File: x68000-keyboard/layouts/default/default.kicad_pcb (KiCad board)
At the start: 2 copper layers, 29.6 x 12.2 mm, 19 parts

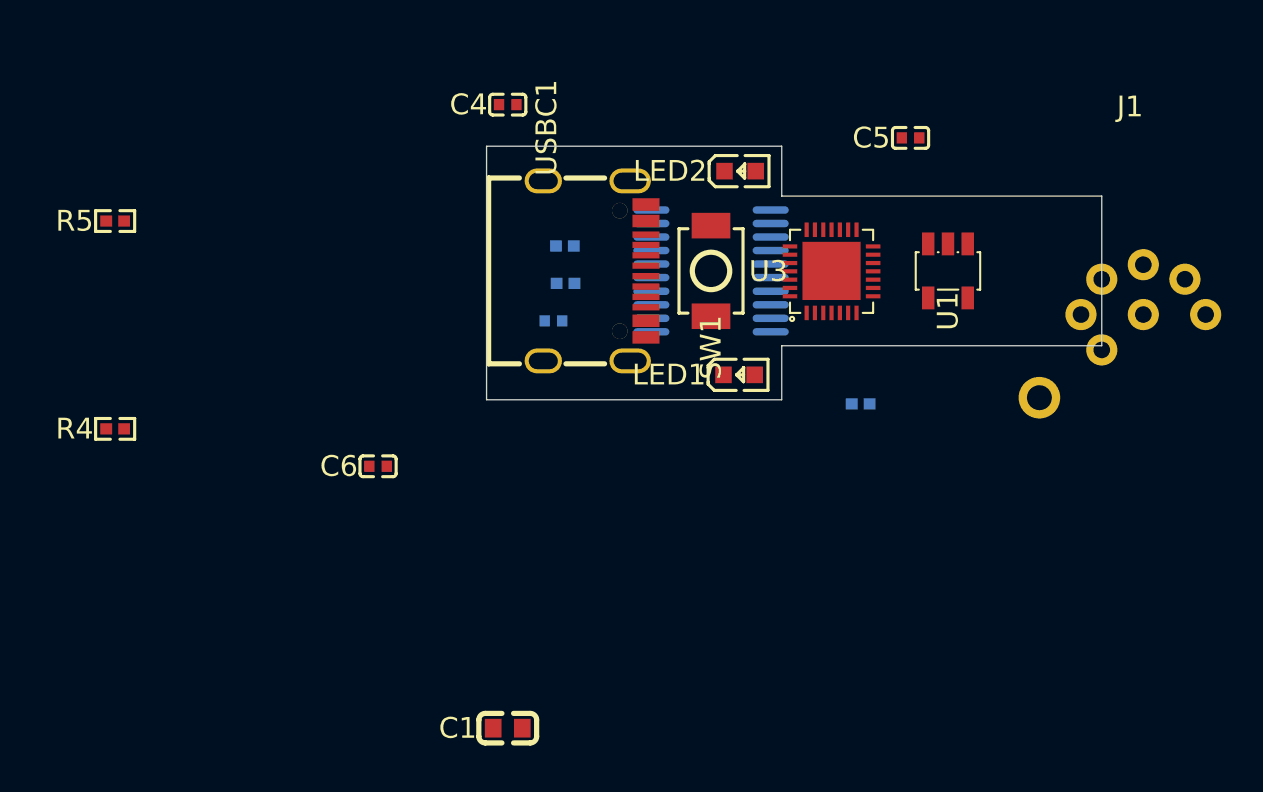
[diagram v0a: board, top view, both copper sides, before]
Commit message: x68000-keyboard: デバッグ LED 削除と Mini-DIN 7pin 自作部品化
- 基板を小型化するためデバッグ LED 2 個と直列抵抗 2 個を削除
  (PB3 / PB4 は未使用ピンとして保留)
- Mini-DIN 7pin プレースホルダを `parts/MiniDIN_7P_X68000/` 専用サブフォルダに
  分離し、自動生成部品と同じ正規構造に整理 (fp-lib-table は atopile が自動登録)
- シールド端子は基板側で用意せず、コネクタ端子の 7 本だけを公開する 7 ピン
  構成に簡略化 (DIN シェルは機構固定金具で十分)

Co-Authored-By: Claude Opus 4.7 (1M context) <noreply@anthropic.com>
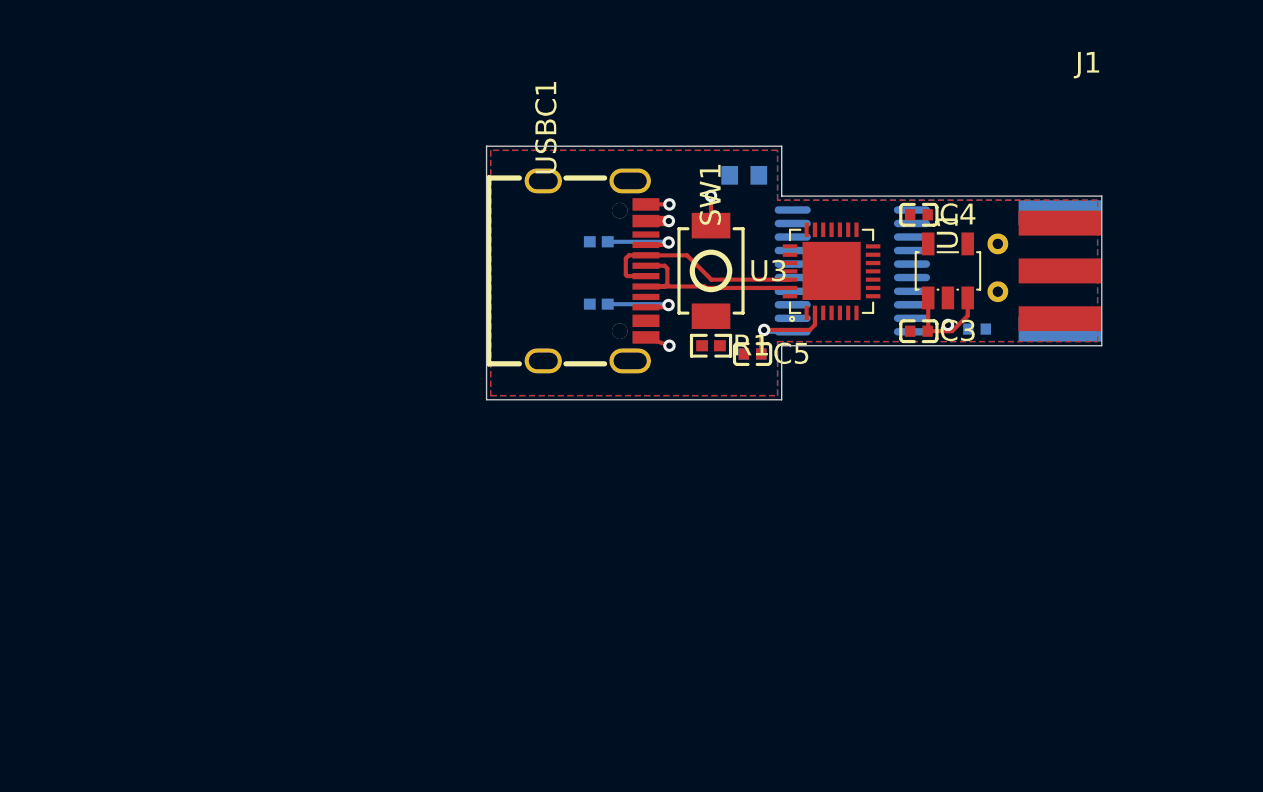
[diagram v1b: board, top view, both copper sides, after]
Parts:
- removed LED1: , Everlight_Elec_19_217_GHC_YR1S2_3T:LED0603-RD
- removed LED2: , Hubei_KENTO_Elec_KT_0603R:LED0603-RD
- removed R4, R5: 470Ω ±1%, UNI_ROYAL_0402WGF4700TCE:R0402
- C1, C6: moved to B.Cu
- C3, R1: moved to F.Cu
- J1: footprint parts:MiniDIN-7P_PLACEHOLDER -> MiniDIN_7P_X68000:MiniDIN_7P_X68000
- moved C6 29.6 mm to (174.0, 98.8)
- moved C1 28.9 mm to (162.8, 91.4), turned to 180 degrees
- moved C4 20.5 mm to (171.2, 93.3), turned to 180 degrees
- moved C3 17.6 mm to (171.2, 98.9)
- moved C5 12.9 mm to (163.2, 100.0), turned to 180 degrees
- moved R1 7.73 mm to (161.2, 99.6)
- moved U2 6.80 mm to (168.0, 96.0)
- moved C2 5.09 mm to (163.2, 100.0)
- moved R3 3.24 mm to (155.8, 97.6)
- moved J1 2.90 mm to (180.0, 96.0)
- moved R2 2.56 mm to (155.8, 94.6)
- turned SW1 to -90 degrees
- turned U1 to -90 degrees
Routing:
- net VBUS: track 0.00 -> 21.5 mm, vias 0 -> 2
- net dn: track 0.00 -> 10.2 mm
- net dp: track 0.00 -> 9.87 mm
- net VDD33: track 0.00 -> 9.50 mm, vias 0 -> 2
- net cc1: track 0.00 -> 4.09 mm, vias 0 -> 1
- net cc2: track 0.00 -> 4.08 mm, vias 0 -> 1
- net GND: track 0.00 -> 2.33 mm, vias 0 -> 2
- added copper zone on B.Cu, net GND
- added copper zone on F.Cu, net GND
- added copper zone on In1.Cu, net GND
- added copper zone on In2.Cu, net VDD33
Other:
- copper layers 2 -> 4

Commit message: 両基板: USB-C CC1/CC2 を MCU PC14/PC15 に接続して USB-PD 検出を有効化
CH32X035 の内蔵 USB-PD コントローラが CC ラインを直接サンプリングできるよう、
従来は 5.1kΩ プルダウンで終端していた CC1/CC2 を MCU の専用ピン PC14 (CC1) /
PC15 (CC2) にも分岐させる。プルダウン経由で 5V 系の Rp 分圧 (max ~1.7V @ 3A
広告) しか印加されないため MCU の絶対最大定格 (VDD+0.3V = 3.6V) は満たされる。

Co-Authored-By: Claude Opus 4.7 (1M context) <noreply@anthropic.com>
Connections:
- R2 pad 1: cc1 -> PC14_CC1_T1C3_T2C2_
- R3 pad 1: cc2 -> PC15_CC2_T2C3_T1ET_
- USBC1 pad A5: cc1 -> PC14_CC1_T1C3_T2C2_
- USBC1 pad B5: cc2 -> PC15_CC2_T2C3_T1ET_
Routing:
- net key_txd: track 0.00 -> 4.09 mm, vias 0 -> 1
- net cc1: track 4.09 -> 0.00 mm, vias 1 -> 0
- net remote: track 0.00 -> 4.08 mm, vias 0 -> 1
- net cc2: track 4.08 -> 0.00 mm, vias 1 -> 0

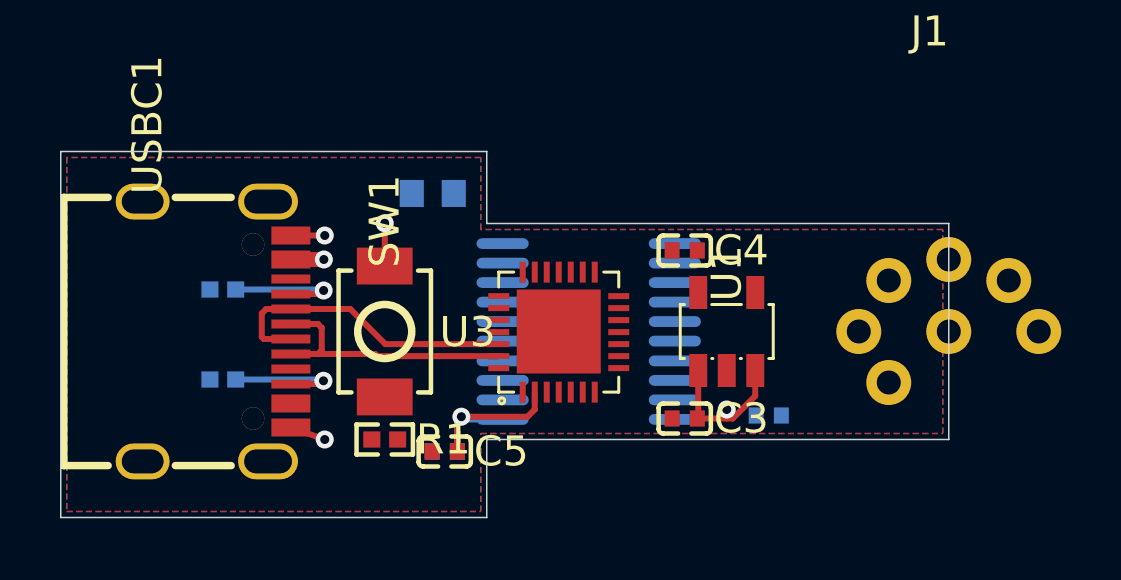
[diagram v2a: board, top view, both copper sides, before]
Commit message: x68000-keyboard: Mini DIN 7pin フットプリントを実物寸法で再描画
Footprint Editor で `MiniDIN_7P_X68000` を本実装に書き直し、PCB 上の J1 も
ライブラリ定義に同期。あわせて、過去の試行錯誤で残っていた失効ライブラリ参照
(`Toshiba_TC7MPB9307FT`、`XKB_Connectivity_TS_1187A_C_6_0_B`、
`YAGEO_RC0603FR_0791KL`) を `fp-lib-table` から除去し、Footprint Editor 起動時の
警告を解消。

Co-Authored-By: Claude Opus 4.7 (1M context) <noreply@anthropic.com>
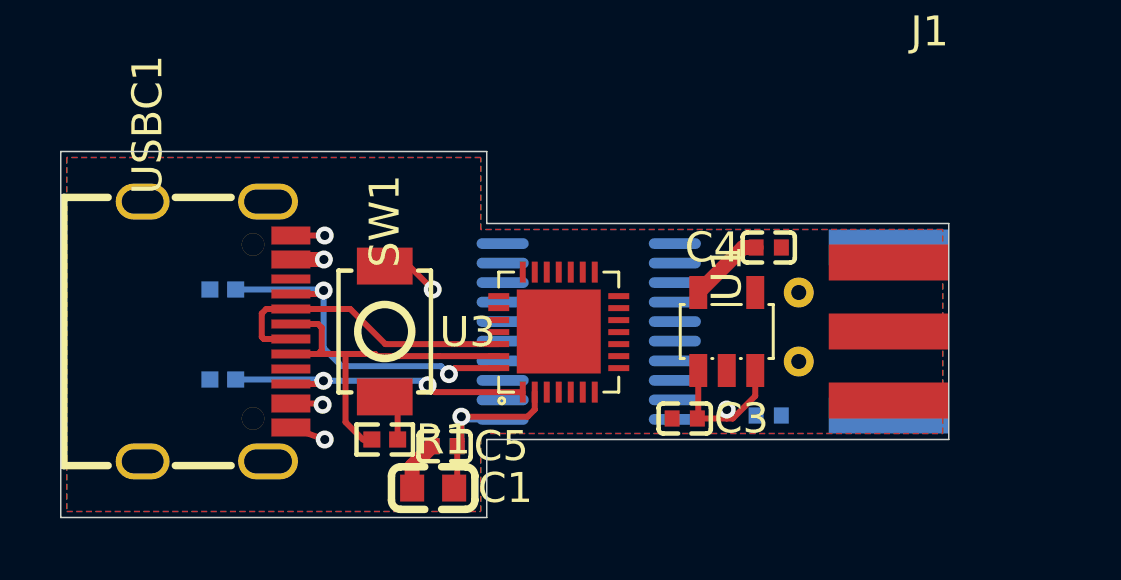
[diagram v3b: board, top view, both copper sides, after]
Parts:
- C1: moved to F.Cu
- moved C1 9.82 mm to (162.8, 101.2)
- moved C4 2.80 mm to (174.0, 93.2), turned to 0 degrees
- moved C2 0.18 mm to (163.2, 99.8)
- moved C5 0.18 mm to (163.2, 99.8)
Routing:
- net PC14_CC1_T1C3_T2C2_: track 0.00 -> 12.3 mm, vias 0 -> 2
- net PC15_CC2_T2C3_T1ET_: track 0.00 -> 10.9 mm, vias 0 -> 2
- net VBUS: track 21.5 -> 11.3 mm, vias 2 -> 3
- net key_txd: track 4.09 -> 0.00 mm, vias 1 -> 0
- net remote: track 4.08 -> 0.00 mm, vias 1 -> 0
- net VDD33: track 9.50 -> 12.9 mm
- net dp: track 9.87 -> 13.3 mm
- net GND: track 2.33 -> 4.00 mm
- net terminal_b: track 0.00 -> 1.60 mm
- added copper zone on In2.Cu, net VBUS
